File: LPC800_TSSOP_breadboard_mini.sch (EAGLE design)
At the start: 16 parts, among them Q1 12MHz

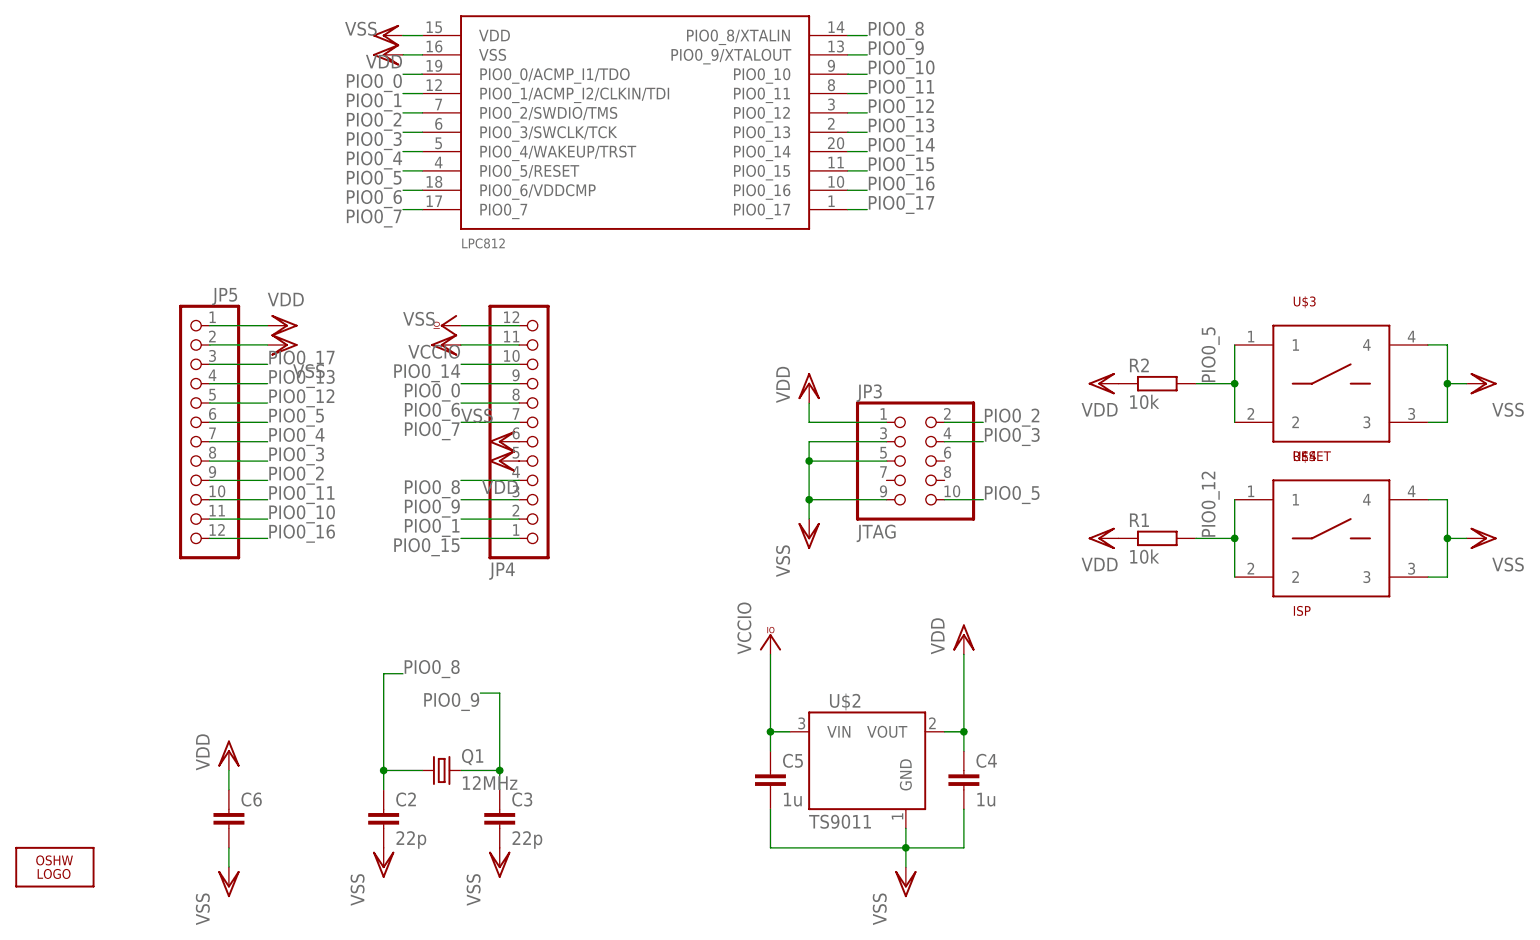
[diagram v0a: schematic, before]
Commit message: * finished LPC800 mini board * fixed pin 1 for JTAG connection - TODO: Printout inspection and checks for the button layout
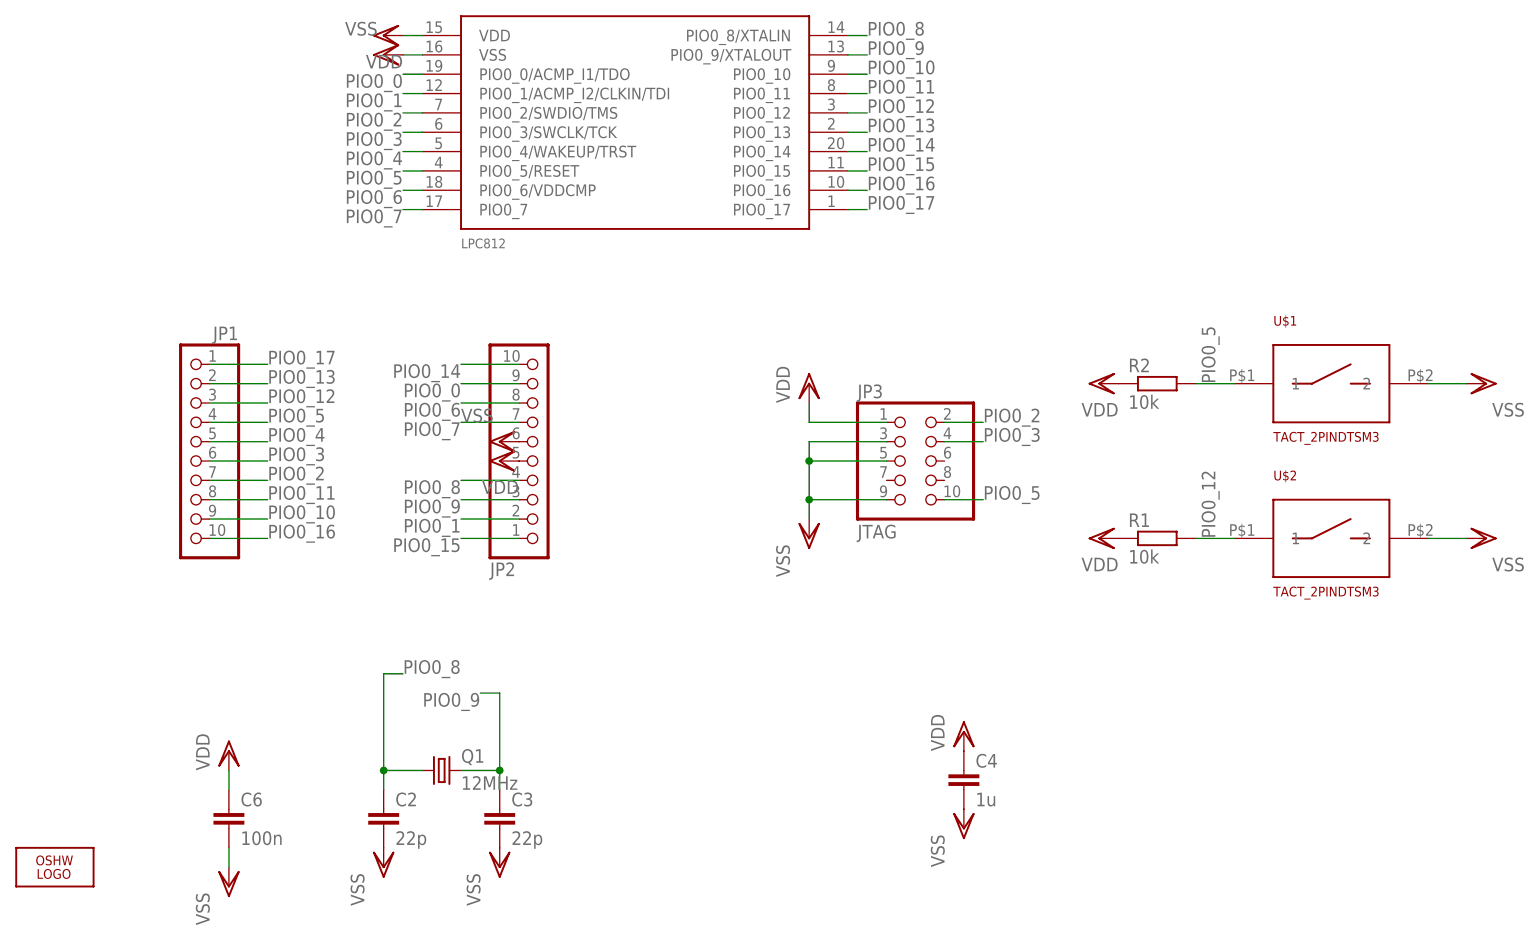
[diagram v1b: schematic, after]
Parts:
- removed C5: 1u, bart_rcl:C-EUC0805K
- removed JP4, JP5: (no value), SquantorConnectors:PINHD-1X12NORM_OCT
- removed U$3: RESET, SquantorButtons:TACT_4PINKMR2
- removed U$4: ISP, SquantorButtons:TACT_4PINKMR2
- added JP1, JP2: (no value), SquantorConnectors:PINHD-1X10NORM_OCT
- added U$1: TACT_2PINDTSM3, SquantorButtons:TACT_2PINDTSM3
- C6: value (none) -> 100n
- U$2: value TS9011 -> TACT_2PINDTSM3; device bart_ic:TS9011 -> SquantorButtons:TACT_2PINDTSM3
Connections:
- removed net VCCIO: C5.1, JP4.12, U$2.VIN
- net PIO0_0: now also JP2.9; no longer JP4.9
- net PIO0_1: now also JP2.2; no longer JP4.2
- net PIO0_10: now also JP1.9; no longer JP5.11
- net PIO0_11: now also JP1.8; no longer JP5.10
- net PIO0_12: now also JP1.3, U$2.1; no longer JP5.5, U$4.1, U$4.2
- net PIO0_13: now also JP1.2; no longer JP5.4
- net PIO0_14: now also JP2.10; no longer JP4.10
- net PIO0_15: now also JP2.1; no longer JP4.1
- net PIO0_16: now also JP1.10; no longer JP5.12
- net PIO0_17: now also JP1.1; no longer JP5.3
- net PIO0_2: now also JP1.7; no longer JP5.9
- net PIO0_3: now also JP1.6; no longer JP5.8
- net PIO0_4: now also JP1.5; no longer JP5.7
- net PIO0_5: now also JP1.4, U$1.1; no longer JP5.6, U$3.1, U$3.2
- net PIO0_6: now also JP2.8; no longer JP4.8
- net PIO0_7: now also JP2.7; no longer JP4.7
- net PIO0_8: now also JP2.4; no longer JP4.4
- net PIO0_9: now also JP2.3; no longer JP4.3
- net VDD: now also JP2.5; no longer JP4.5, JP5.1, U$2.VOUT
- net VSS: now also JP2.6, U$1.2, U$2.2; no longer C5.2, JP4.11, JP4.6, JP5.2, U$2.GND, U$3.3, U$3.4, U$4.3, U$4.4
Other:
- moved on the sheet: U$2

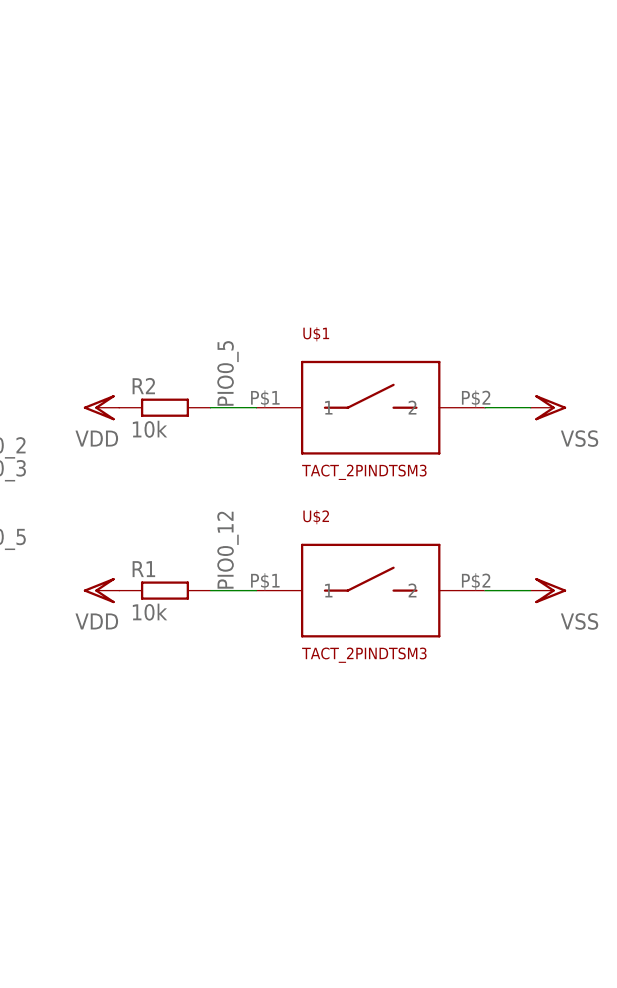
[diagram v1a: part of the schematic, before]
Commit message: * updated boards with cheaper buttons, better layout and indexed JTAG header
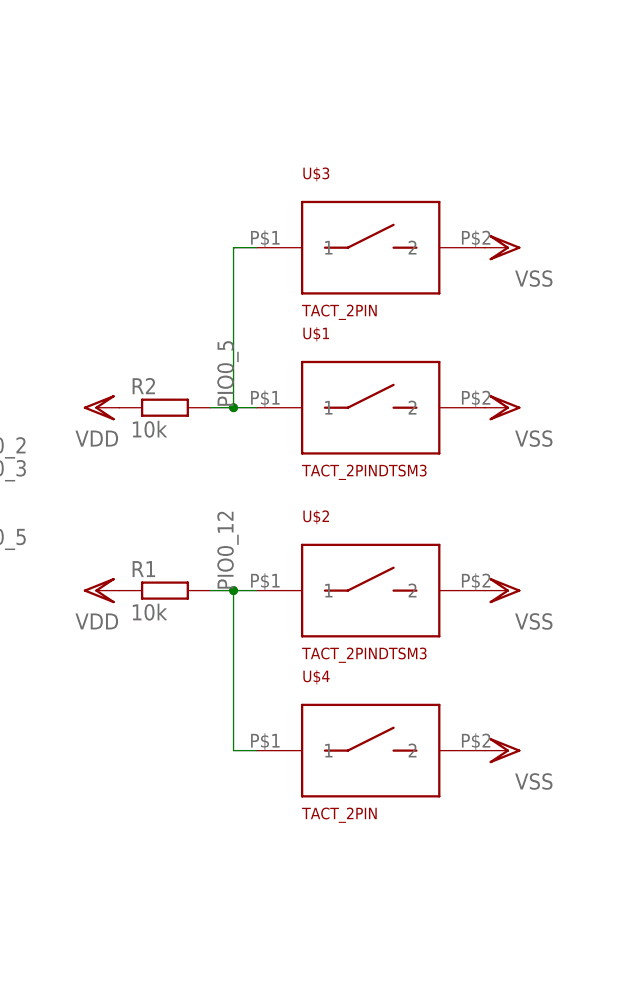
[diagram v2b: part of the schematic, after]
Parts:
- added U$3, U$4: TACT_2PIN, SquantorButtons:TACT_2PIN
- JP3: device bart_connectors:PINHD-2X5SMD_1.27_SMD -> SquantorConnectors:PINHD-2X5SMD_1.27_SMD
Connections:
- net PIO0_12: now also U$4.1
- net PIO0_5: now also U$3.1
- net VSS: now also U$3.2, U$4.2
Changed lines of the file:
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@@
 <?xml version="1.0" encoding="utf-8"?>
 <!DOCTYPE eagle SYSTEM "eagle.dtd">
-<eagle version="7.1.0">
+<eagle version="6.5.0">
 <drawing>
 <settings>
@@
 <part name="VSS5" library="supply1" deviceset="VSS" device=""/>
 <part name="VDD3" library="supply1" deviceset="VDD" device=""/>
-<part name="JP3" library="bart_connectors" deviceset="PINHD-2X5" device="SMD_1.27_SMD" value="JTAG"/>
+<part name="JP3" library="SquantorConnectors" deviceset="PINHD-2X5" device="SMD_1.27_SMD" value="JTAG"/>
 <part name="VDD4" library="supply1" deviceset="VDD" device=""/>
 <part name="VSS6" library="supply1" deviceset="VSS" device=""/>
@@
 <part name="U$1" library="SquantorButtons" deviceset="TACT_2PIN" device="DTSM3"/>
 <part name="U$2" library="SquantorButtons" deviceset="TACT_2PIN" device="DTSM3"/>
+<part name="U$3" library="SquantorButtons" deviceset="TACT_2PIN" device=""/>
+<part name="U$4" library="SquantorButtons" deviceset="TACT_2PIN" device=""/>
+<part name="VSS1" library="supply1" deviceset="VSS" device=""/>
+<part name="VSS8" library="supply1" deviceset="VSS" device=""/>
 </parts>
 <sheets>
@@
 <instance part="VSS7" gate="G$1" x="63.5" y="58.42" rot="R270"/>
 <instance part="VDD2" gate="G$1" x="63.5" y="55.88" rot="R90"/>
-<instance part="VSS9" gate="G$1" x="193.04" y="66.04" rot="R90"/>
-<instance part="VSS10" gate="G$1" x="193.04" y="45.72" rot="R90"/>
+<instance part="VSS9" gate="G$1" x="187.96" y="66.04" rot="R90"/>
+<instance part="VSS10" gate="G$1" x="187.96" y="45.72" rot="R90"/>
 <instance part="R1" gate="G$1" x="149.86" y="45.72"/>
 <instance part="R2" gate="G$1" x="149.86" y="66.04"/>
@@
 <instance part="U$1" gate="G$1" x="172.72" y="66.04"/>
 <instance part="U$2" gate="G$1" x="172.72" y="45.72"/>
+<instance part="U$3" gate="G$1" x="172.72" y="83.82"/>
+<instance part="U$4" gate="G$1" x="172.72" y="27.94"/>
+<instance part="VSS1" gate="G$1" x="187.96" y="27.94" rot="R90"/>
+<instance part="VSS8" gate="G$1" x="187.96" y="83.82" rot="R90"/>
 </instances>
 <busses>
@@
 <pinref part="VSS9" gate="G$1" pin="VSS"/>
 <pinref part="U$1" gate="G$1" pin="2"/>
-<wire x1="190.5" y1="66.04" x2="185.42" y2="66.04" width="0.1524" layer="91"/>
 </segment>
 <segment>
 <pinref part="VSS10" gate="G$1" pin="VSS"/>
 <pinref part="U$2" gate="G$1" pin="2"/>
-<wire x1="190.5" y1="45.72" x2="185.42" y2="45.72" width="0.1524" layer="91"/>
 </segment>
 <segment>
@@
 <pinref part="VSS11" gate="G$1" pin="VSS"/>
 <wire x1="27.94" y1="5.08" x2="27.94" y2="2.54" width="0.1524" layer="91"/>
+</segment>
+<segment>
+<pinref part="U$4" gate="G$1" pin="2"/>
+<pinref part="VSS1" gate="G$1" pin="VSS"/>
+</segment>
+<segment>
+<pinref part="U$3" gate="G$1" pin="2"/>
+<pinref part="VSS8" gate="G$1" pin="VSS"/>
 </segment>
 </net>
@@
 <segment>
 <pinref part="R2" gate="G$1" pin="2"/>
-<wire x1="154.94" y1="66.04" x2="160.02" y2="66.04" width="0.1524" layer="91"/>
+<wire x1="154.94" y1="66.04" x2="157.48" y2="66.04" width="0.1524" layer="91"/>
 <label x="157.48" y="66.04" size="1.778" layer="95" rot="R90"/>
 <pinref part="U$1" gate="G$1" pin="1"/>
+<pinref part="U$3" gate="G$1" pin="1"/>
+<wire x1="157.48" y1="66.04" x2="160.02" y2="66.04" width="0.1524" layer="91"/>
+<wire x1="160.02" y1="83.82" x2="157.48" y2="83.82" width="0.1524" layer="91"/>
+<wire x1="157.48" y1="83.82" x2="157.48" y2="66.04" width="0.1524" layer="91"/>
+<junction x="157.48" y="66.04"/>
 </segment>
 </net>
@@
 <segment>
 <pinref part="R1" gate="G$1" pin="2"/>
-<wire x1="154.94" y1="45.72" x2="160.02" y2="45.72" width="0.1524" layer="91"/>
+<wire x1="154.94" y1="45.72" x2="157.48" y2="45.72" width="0.1524" layer="91"/>
 <label x="157.48" y="45.72" size="1.778" layer="95" rot="R90"/>
 <pinref part="U$2" gate="G$1" pin="1"/>
-</segment>
-</net>
+<pinref part="U$4" gate="G$1" pin="1"/>
+<wire x1="157.48" y1="45.72" x2="160.02" y2="45.72" width="0.1524" layer="91"/>
+<wire x1="160.02" y1="27.94" x2="157.48" y2="27.94" width="0.1524" layer="91"/>
+<wire x1="157.48" y1="27.94" x2="157.48" y2="45.72" width="0.1524" layer="91"/>
+<junction x="157.48" y="45.72"/>
+</segment>
+</net>
